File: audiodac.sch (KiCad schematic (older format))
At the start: 2 parts

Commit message: Main Board Rev A files
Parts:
- removed U?: TLV320AIC23BRHD, Package_DFN_QFN:QFN-28-1EP_5x5mm_P0.5mm_EP3.35x3.35mm, symbol Audio:TLV320AIC23BRHD
- added C10: 1uF, Capacitor_SMD:C_0603_1608Metric, symbol Device:C
- added C4: 100nF, Capacitor_SMD:C_0603_1608Metric, symbol Device:C
- added U4: SGTL5000XNLA3, Package_DFN_QFN:QFN-20-1EP_3x3mm_P0.4mm_EP1.65x1.65mm, symbol Audio:SGTL5000XNLA3
- added U5: MIC5504-1.8YM5, Package_TO_SOT_SMD:SOT-23-5, symbol Regulator_Linear:MIC5504-1.8YM5
- gave numbers to parts that had none: 1
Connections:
- net labels added: +1V8, HP_L, HP_R, HP_VGND, I2C_LRCIN, I2S_BCLK, I2S_DIN, I2S_DOUT, SCL, SDA, SYS_MCLK, VAG
- net labels removed: BCLK, DIN, DOUT, LRCIN, LRCOUT, MODE, SCLK, SDIN, ~CS
- wire segments 26 -> 35
- no-connect marks 0 -> 7
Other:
- note added: "VDDA can be connected to 1.8V or 3.3V,\nbut 3.3V is easier / lower loss."
- moved on the sheet: C3

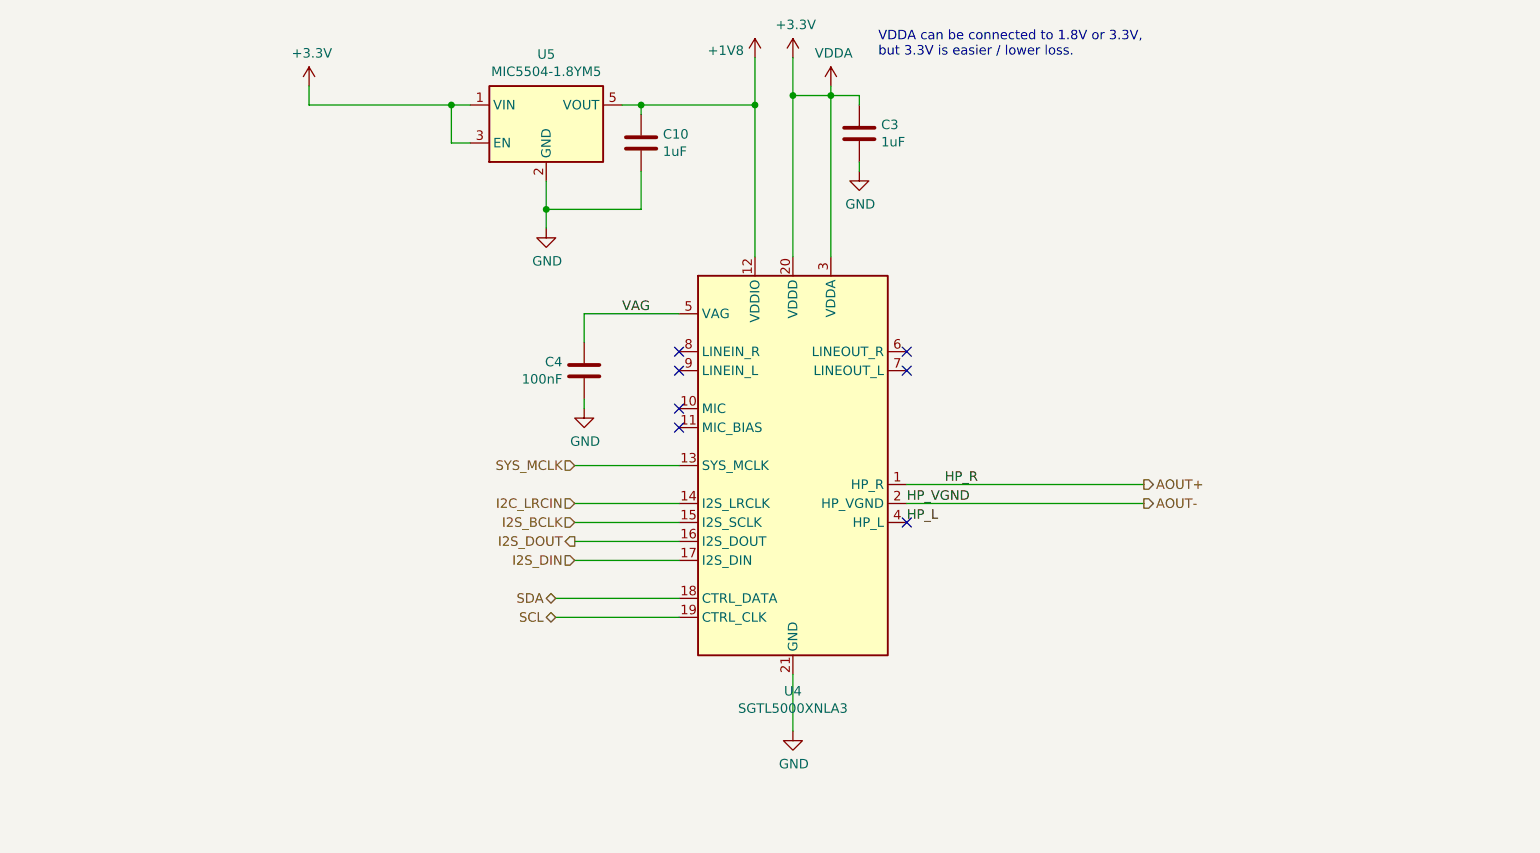
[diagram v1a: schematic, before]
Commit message: Rev B Portal Gun Mainboard as ordered
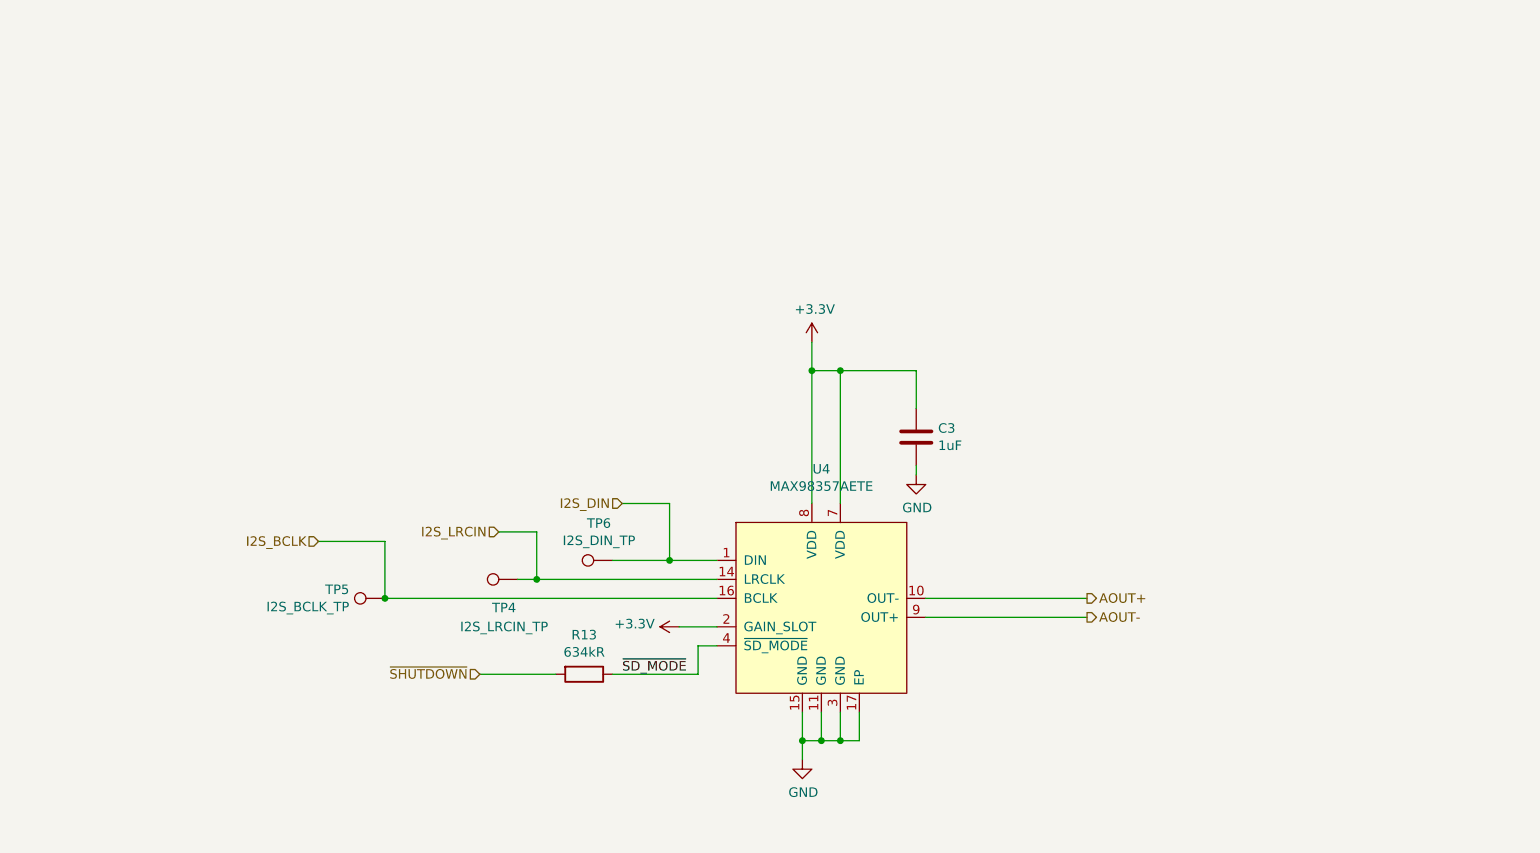
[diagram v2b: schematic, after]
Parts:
- removed C10: 1uF, Capacitor_SMD:C_0603_1608Metric, symbol Device:C
- removed C4: 100nF, Capacitor_SMD:C_0603_1608Metric, symbol Device:C
- removed U4: SGTL5000XNLA3, Package_DFN_QFN:QFN-20-1EP_3x3mm_P0.4mm_EP1.65x1.65mm, symbol Audio:SGTL5000XNLA3
- removed U5: MIC5504-1.8YM5, Package_TO_SOT_SMD:SOT-23-5, symbol Regulator_Linear:MIC5504-1.8YM5
- added R13: 634kR, Resistor_SMD:R_0603_1608Metric, symbol Device:R
- added TP4: I2S_LRCIN_TP, TestPoint:TestPoint_Pad_D1.5mm, symbol Connector:TestPoint
- added TP5: I2S_BCLK_TP, TestPoint:TestPoint_Pad_D1.5mm, symbol Connector:TestPoint
- added TP6: I2S_DIN_TP, TestPoint:TestPoint_Pad_D1.5mm, symbol Connector:TestPoint
- added U4: MAX98357AETE, Package_DFN_QFN:TQFN-16-1EP_3x3mm_P0.5mm_EP1.23x1.23mm, symbol AudioDac:MAX98357AETE
- C3: footprint Capacitor_SMD:C_0603_1608Metric -> Capacitor_SMD:C_0805_2012Metric
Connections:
- net +3V3: now also U4.2 (GAIN_SLOT), U4.7 (VDD), U4.8 (VDD)
- net AOUT+: now also U4.10 (OUT-)
- net AOUT-: now also U4.9 (OUT+)
- net GND: now also U4.11 (GND), U4.15 (GND), U4.17 (EP), U4.3 (GND)
- net I2S_BCLK: now also TP5.1, U4.16 (BCLK)
- net I2S_DIN: now also TP6.1, U4.1 (DIN)
- new net I2S_LRCIN: TP4.1, U4.14 (LRCLK)
- new net ~SD_MODE: R13.1, U4.4 (~SD_MODE)
- new net ~SHUTDOWN: R13.2
- no-connect marks 7 -> 0
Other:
- note removed: "VDDA can be connected to 1.8V or 3.3V,\nbut 3.3V is easier / lower loss."
- moved on the sheet: C3

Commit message: Updates. Firmware running on main board rev B
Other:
- note added: "12"
- note added: "15"
- note added: "3"
- note added: "6"
- note added: "9"
- note added: "Connect to GND\nthrough 100kR"
- note added: "Drive SD_MODE high through a sufficiently large resistor to select both the left\nand right words of the stereo input data (left/2 + right/2).\nRLARGE and RSMALL are determined by the VDDIO voltage (logic\nvoltage from control interface) that is driving SD_MODE \naccording to the following two equations:\nRSMALL (kΩ) = 94.0 x VDDIO - 100\nRLARGE (kΩ) = 222.2 x VDDIO - 100"
- note added: "GAIN_SLOT"
- note added: "GND"
- note added: "I2S Gain (dB)"
- note added: "NC"
- note added: "VDD"
- note added: "VDD through\n100kR resitor"
- moved on the sheet: R13, TP4, TP5, TP6
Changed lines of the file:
@@
 Comment4 ""
 $EndDescr
-Text HLabel 8300 4100 2    50   Output ~ 0
+Text HLabel 7600 4100 2    50   Output ~ 0
 AOUT+
-Text HLabel 8300 4200 2    50   Output ~ 0
+Text HLabel 7600 4200 2    50   Output ~ 0
 AOUT-
 Wire Wire Line
-	7450 4200 8300 4200
-Text HLabel 5200 3750 0    50   Input ~ 0
+	7450 4200 7600 4200
+Text HLabel 4850 3900 0    50   Input ~ 0
 I2S_LRCIN
-Text HLabel 4250 3800 0    50   Input ~ 0
+Text HLabel 4850 4000 0    50   Input ~ 0
 I2S_BCLK
 $Comp
 L power:+3.3V #PWR0119
 U 1 1 6029BD20
-P 6850 2750
-F 0 "#PWR0119" H 6850 2600 50  0001 C CNN
-F 1 "+3.3V" H 6865 2923 50  0000 C CNN
-F 2 "" H 6850 2750 50  0001 C CNN
-F 3 "" H 6850 2750 50  0001 C CNN
-	1    6850 2750
+P 6850 2850
+F 0 "#PWR0119" H 6850 2700 50  0001 C CNN
+F 1 "+3.3V" H 6865 3023 50  0000 C CNN
+F 2 "" H 6850 2850 50  0001 C CNN
+F 3 "" H 6850 2850 50  0001 C CNN
+	1    6850 2850
 	1    0    0    -1
 $EndComp
@@
 $EndComp
 Wire Wire Line
-	7450 4100 8300 4100
-Text HLabel 5850 3600 0    50   Input ~ 0
+	7450 4100 7600 4100
+Text HLabel 4850 3800 0    50   Input ~ 0
 I2S_DIN
 Wire Wire Line
-	5400 4000 6350 4000
+	5550 4000 6350 4000
 $Comp
 L Connector:TestPoint TP4
 U 1 1 60750D00
-P 5300 4000
-F 0 "TP4" V 5450 4072 50  0000 C CNN
-F 1 "I2S_LRCIN_TP" V 5550 4072 50  0000 C CNN
-F 2 "TestPoint:TestPoint_Pad_D1.5mm" H 5500 4000 50  0001 C CNN
-F 3 "~" H 5500 4000 50  0001 C CNN
-	1    5300 4000
+P 5450 4000
+F 0 "TP4" V 5255 4072 50  0000 C CNN
+F 1 "I2S_LRCIN_TP" V 5346 4072 50  0000 C CNN
+F 2 "TestPoint:TestPoint_Pad_D1.5mm" H 5650 4000 50  0001 C CNN
+F 3 "~" H 5650 4000 50  0001 C CNN
+	1    5450 4000
 	0    -1   1    0
 $EndComp
-Connection ~ 5400 4000
-Wire Wire Line
-	5400 3750 5400 4000
-Wire Wire Line
-	5200 3750 5400 3750
-Wire Wire Line
-	4250 3800 4600 3800
-Wire Wire Line
-	4600 3800 4600 4100
-Wire Wire Line
-	4600 4100 6350 4100
+Connection ~ 5550 4000
+Wire Wire Line
+	5550 3900 5550 4000
+Wire Wire Line
+	4850 3900 5550 3900
+Wire Wire Line
+	4850 4000 5200 4000
+Wire Wire Line
+	5200 4000 5200 4100
+Wire Wire Line
+	5200 4100 6350 4100
 $Comp
 L Connector:TestPoint TP5
 U 1 1 6075ABC0
-P 4600 4100
-F 0 "TP5" V 4646 4288 50  0000 L CNN
-F 1 "I2S_BCLK_TP" V 4555 4288 50  0000 L CNN
-F 2 "TestPoint:TestPoint_Pad_D1.5mm" H 4800 4100 50  0001 C CNN
-F 3 "~" H 4800 4100 50  0001 C CNN
-	1    4600 4100
+P 5200 4100
+F 0 "TP5" V 5246 4288 50  0000 L CNN
+F 1 "I2S_BCLK_TP" V 5155 4288 50  0000 L CNN
+F 2 "TestPoint:TestPoint_Pad_D1.5mm" H 5400 4100 50  0001 C CNN
+F 3 "~" H 5400 4100 50  0001 C CNN
+	1    5200 4100
 	0    -1   -1   0
 $EndComp
-Connection ~ 4600 4100
-Wire Wire Line
-	5850 3600 6100 3600
+Connection ~ 5200 4100
+Wire Wire Line
+	4850 3800 6100 3800
 $Comp
 L AudioDac:MAX98357AETE U4
@@
 	6800 4700 6800 4850
 Wire Wire Line
-	6850 3600 6850 2900
-Wire Wire Line
-	6850 2900 7000 2900
-Wire Wire Line
-	7400 2900 7400 3100
-Wire Wire Line
-	7000 3600 7000 2900
-Connection ~ 7000 2900
-Wire Wire Line
-	7000 2900 7400 2900
-Connection ~ 6850 2900
-Wire Wire Line
-	6850 2750 6850 2900
+	6850 3600 6850 3000
+Wire Wire Line
+	6850 3000 7000 3000
+Wire Wire Line
+	7400 3000 7400 3100
+Wire Wire Line
+	7000 3600 7000 3000
+Connection ~ 7000 3000
+Wire Wire Line
+	7000 3000 7400 3000
+Connection ~ 6850 3000
+Wire Wire Line
+	6850 2850 6850 3000
 Wire Wire Line
 	6900 4850 6900 4700
@@
 	7000 4850 7000 4700
 Connection ~ 6900 4850
-Text HLabel 5100 4500 0    50   Input ~ 0
+Text HLabel 4850 4350 0    50   Input ~ 0
 ~SHUTDOWN
 Wire Wire Line
-	6250 4500 6250 4350
-Wire Wire Line
-	6250 4350 6350 4350
-Wire Wire Line
-	5100 4500 5500 4500
+	4850 4350 5100 4350
 $Comp
 L power:+3.3V #PWR0104
 U 1 1 60D4805E
-P 6150 4250
-F 0 "#PWR0104" H 6150 4100 50  0001 C CNN
-F 1 "+3.3V" V 6165 4378 50  0000 L CNN
-F 2 "" H 6150 4250 50  0001 C CNN
-F 3 "" H 6150 4250 50  0001 C CNN
-	1    6150 4250
+P 6300 4250
+F 0 "#PWR0104" H 6300 4100 50  0001 C CNN
+F 1 "+3.3V" V 6315 4378 50  0000 L CNN
+F 2 "" H 6300 4250 50  0001 C CNN
+F 3 "" H 6300 4250 50  0001 C CNN
+	1    6300 4250
 	0    -1   -1   0
 $EndComp
 Wire Wire Line
-	6150 4250 6350 4250
+	6300 4250 6350 4250
 Wire Wire Line
 	6100 3900 6350 3900
-Connection ~ 6100 3900
-Wire Wire Line
-	6100 3600 6100 3900
+Wire Wire Line
+	6100 3800 6100 3900
 $Comp
 L Connector:TestPoint TP6
 U 1 1 6075DC2A
-P 5800 3900
-F 0 "TP6" V 5605 3972 50  0000 C CNN
-F 1 "I2S_DIN_TP" V 5696 3972 50  0000 C CNN
-F 2 "TestPoint:TestPoint_Pad_D1.5mm" H 6000 3900 50  0001 C CNN
-F 3 "~" H 6000 3900 50  0001 C CNN
-	1    5800 3900
-	0    -1   1    0
-$EndComp
-Wire Wire Line
-	5800 3900 6100 3900
-Wire Wire Line
-	5300 4000 5400 4000
+P 6100 3800
+F 0 "TP6" H 6100 4125 50  0000 C CNN
+F 1 "I2S_DIN_TP" H 6100 4034 50  0000 C CNN
+F 2 "TestPoint:TestPoint_Pad_D1.5mm" H 6300 3800 50  0001 C CNN
+F 3 "~" H 6300 3800 50  0001 C CNN
+	1    6100 3800
+	-1   0    0    -1
+$EndComp
+Wire Wire Line
+	5450 4000 5550 4000
 $Comp
 L Device:R R13
 U 1 1 60D8CBB8
-P 5650 4500
-F 0 "R13" V 5443 4500 50  0000 C CNN
-F 1 "634kR" V 5534 4500 50  0000 C CNN
-F 2 "Resistor_SMD:R_0603_1608Metric" V 5580 4500 50  0001 C CNN
-F 3 "~" H 5650 4500 50  0001 C CNN
-	1    5650 4500
+P 5250 4350
+F 0 "R13" V 5043 4350 50  0000 C CNN
+F 1 "634kR" V 5134 4350 50  0000 C CNN
+F 2 "Resistor_SMD:R_0603_1608Metric" V 5180 4350 50  0001 C CNN
+F 3 "~" H 5250 4350 50  0001 C CNN
+	1    5250 4350
 	0    1    1    0
 $EndComp
-Wire Wire Line
-	5800 4500 6250 4500
-Text Label 5850 4500 0    50   ~ 0
+Text Label 5550 4350 0    50   ~ 0
 ~SD_MODE
 Wire Wire Line
@@
 	7100 4850 7100 4700
 Connection ~ 7000 4850
+Connection ~ 6100 3800
+Wire Wire Line
+	5400 4350 6350 4350
+Text Notes 3150 5350 0    50   ~ 0
+Drive  SD_MODE high  through  a  sufficiently  large  resistor  to  select  both  the  left\nand  right  words  of  the  stereo  input  data  (left/2  +  right/2).\nRLARGE  and  RSMALL are determined by the VDDIO voltage (logic\nvoltage from control  interface)  that  is  driving  SD_MODE \naccording  to  the following two equations:\nRSMALL (kΩ) = 94.0 x VDDIO - 100\nRLARGE (kΩ) = 222.2 x VDDIO - 100
+Text Notes 2700 3150 0    50   ~ 0
+GAIN_SLOT
+Text Notes 3400 3150 0    50   ~ 0
+I2S Gain (dB)
+Wire Notes Line
+	2650 3200 3950 3200
+Wire Notes Line
+	3350 3100 3350 4100
+Text Notes 2700 3400 0    50   ~ 0
+Connect to GND\nthrough 100kR
+Text Notes 3500 3350 0    50   ~ 0
+15
+Text Notes 2900 3550 0    50   ~ 0
+GND
+Text Notes 3500 3550 0    50   ~ 0
+12
+Text Notes 2900 3700 0    50   ~ 0
+NC
+Text Notes 3500 3700 0    50   ~ 0
+9
+Text Notes 2900 3850 0    50   ~ 0
+VDD
+Text Notes 3500 3850 0    50   ~ 0
+6
+Text Notes 2700 4050 0    50   ~ 0
+VDD through\n100kR resitor
+Text Notes 3500 4050 0    50   ~ 0
+3
 $EndSCHEMATC
